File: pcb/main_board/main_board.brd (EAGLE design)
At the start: 72.4 x 72.4 mm, 30 parts, among them J1 5025700893, P1 53398-0510, P2 53398-0810, P3 53398-0410, U1 ATSAMD51J19A-AUT, U13 SPX3819-3.3, X2 32.768, X3 microUSB

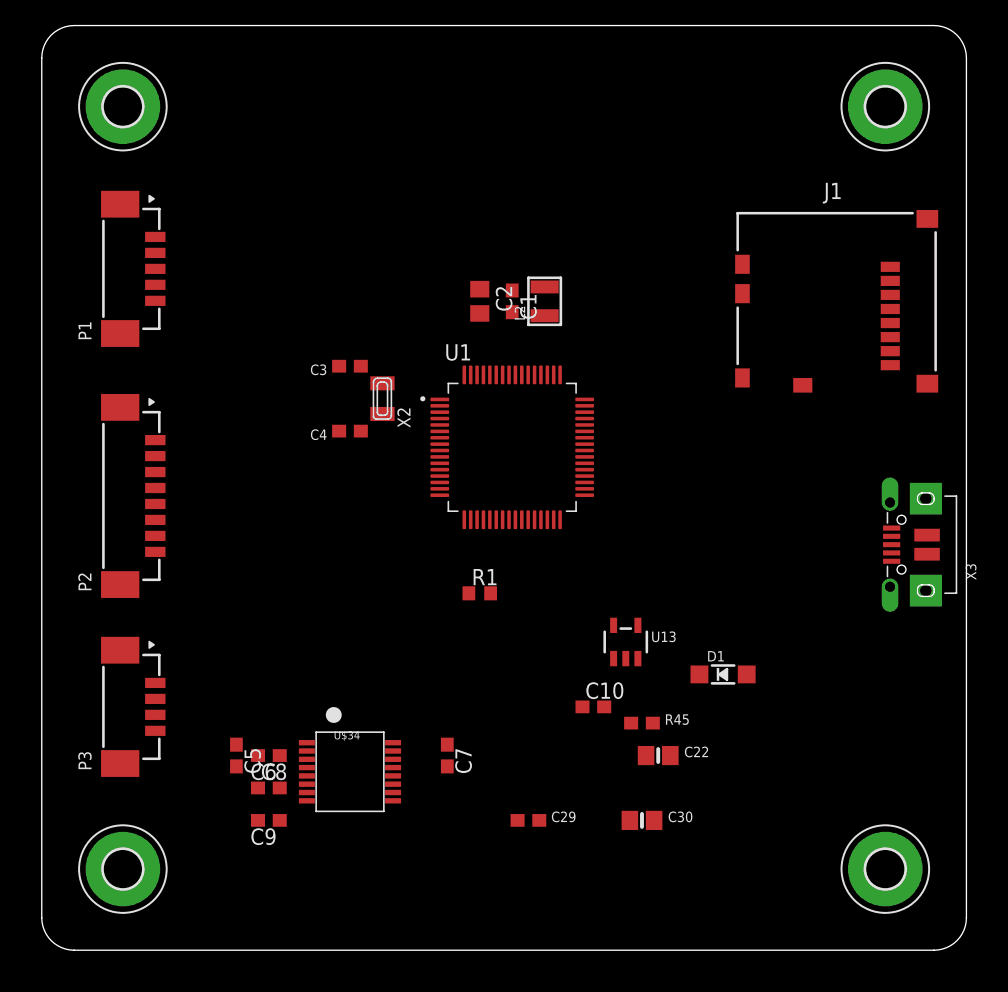
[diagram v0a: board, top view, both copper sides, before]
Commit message: moved to feather wing design
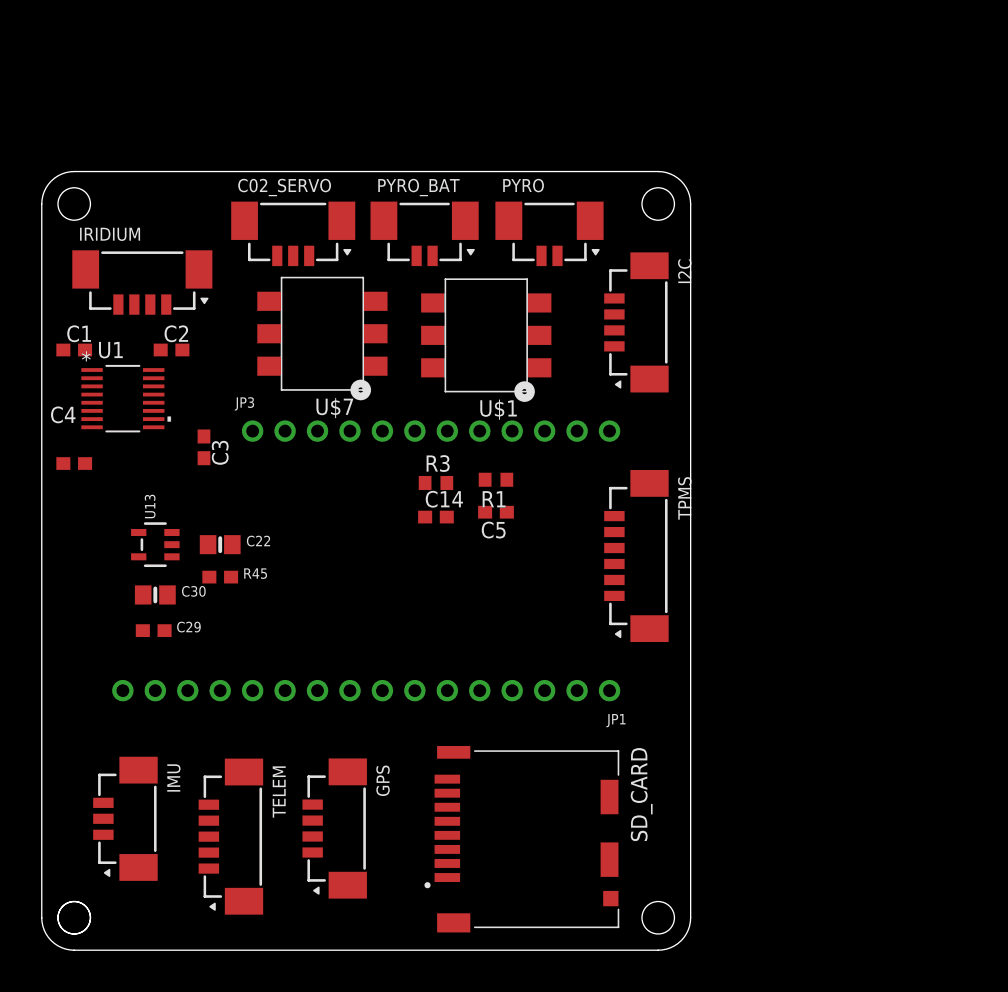
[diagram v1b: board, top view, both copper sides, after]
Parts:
- removed C10: 1uF, rcl:C0603
- removed C6, C7, C8: 0.1uF, rcl:C0603
- removed C9: 0.01uF, rcl:C0603
- removed D1: MBR120, microbuilder:SOD-123
- removed H1, H2, H3, H4: MOUNT-PAD-ROUND3.0, holes:3,0-PAD
- removed J1: 5025700893, 5025700893:MOLEX_5025700893
- removed L2: 10uH, microbuilder:INDUCTOR_1007
- removed P1: 53398-0510, con-molex-picoblade:53398-0510
- removed P2: 53398-0810, con-molex-picoblade:53398-0810
- removed P3: 53398-0410, con-molex-picoblade:53398-0410
- removed U$34: MAX3232E, TI_radio:SSOP-16
- removed X2: 32.768, adafruit2:XTAL3215
- removed X3: microUSB, microbuilder:4UCONN_20329_V2
- added C02_SERVO, IMU: 53398-0310, con-molex-picoblade:53398-0310
- added C14: 0.1uF, adafruit:C0603
- added GPS, I2C, IRIDIUM: 53398-0410, con-molex-picoblade:53398-0410
- added JP1: (no value), microbuilder:1X16_ROUND
- added JP3: (no value), microbuilder:1X12_ROUND
- added PYRO, PYRO_BAT: 53398-0210, con-molex-picoblade:53398-0210
- added R3: 288, adafruit:R0603
- added SD_CARD: DM3CS-SF, DM3CS-SF:HRS_DM3CS-SF
- added TELEM: 53398-0510, con-molex-picoblade:53398-0510
- added TPMS: 53398-0610, con-molex-picoblade:53398-0610
- added U$1, U$7: AQV252GA, TI_radio:DIP6
- C1: value 1uF -> 0.1uF
- C2: value 10uF -> 0.1uF; device rcl:C0805 -> rcl:C0603
- C3, C4: value 22pF -> 0.1uF; device microbuilder:0603-NO -> rcl:C0603
- C5: device rcl:C0603 -> adafruit:C0603
- R1: value 10k -> 288; device rcl:R0603 -> adafruit:R0603
- U1: value ATSAMD51J19A-AUT -> ADM3101EARQZ-REELRQ_16_ADI-L; device ATSAMD51J19A-AUT:QFP50P1200X1200X120-64N -> ADM310:RQ_16_ADI-L
- moved C30 42.0 mm to (8.89, 27.8)
- moved C22 38.1 mm to (14.0, 31.8)
- moved U13 37.6 mm to (8.89, 31.8), turned to 90 degrees
- moved R45 34.9 mm to (14.0, 29.2)
- moved C1 34.5 mm to (2.54, 47.0), turned to 0 degrees
- moved C29 32.9 mm to (8.76, 25.0)
- moved U1 30.7 mm to (6.35, 43.2)
- moved C5 27.9 mm to (35.6, 34.3), turned to 180 degrees
- moved C2 24.4 mm to (10.2, 47.0), turned to 0 degrees
- moved C4 21.7 mm to (2.54, 38.1), turned to 0 degrees
- moved C3 13.1 mm to (12.7, 39.4), turned to 270 degrees
- moved R1 8.98 mm to (35.6, 36.8), turned to 180 degrees
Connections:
- removed net 3.3V: C7.1, U$34.16
- removed net D+: U1.46, X3.D+
- removed net D-: U1.45, X3.D-
- removed net N$11: J1.2
- removed net N$12: J1.1
- removed net N$13: J1.8
- removed net N$14: J1.7
- removed net N$15: P1.2
- removed net N$16: P1.3
- removed net N$17: P1.4
- removed net N$18: P1.5
- removed net N$19: H2.B3,0
- removed net N$2: P1.1
- removed net N$20: H1.B3,0
- removed net N$21: H4.B3,0
- removed net N$22: H3.B3,0
- removed net N$23: P2.1
- removed net N$24: P2.2
- removed net N$25: P2.3
- removed net N$26: P2.4
- removed net N$27: P2.5
- removed net N$28: P2.6
- removed net N$29: P2.7
- removed net N$30: P2.8
- removed net N$31: P3.1
- removed net N$32: P3.2
- removed net N$33: P3.3
- removed net N$34: P3.4
- removed net N$35: C5.1, U$34.1
- removed net N$36: C5.2, U$34.3
- removed net N$37: C8.1, U$34.4
- removed net N$38: C8.2, U$34.5
- removed net N$39: C9.1, U$34.6
- removed net N$40: C6.1, U$34.2
- removed net N$41: C10.2, U1.4
- removed net N$5: C3.1, U1.1, X2.P$1
- removed net QSPI_CS: U1.24
- removed net QSPI_DATA[0]: U1.17
- removed net QSPI_DATA[1]: U1.18
- removed net QSPI_DATA[2]: U1.19
- removed net QSPI_DATA[3]: U1.20
- removed net QSPI_SCK: U1.23
- removed net RX0: U1.40
- removed net SD_DET: J1.10
- removed net SWCLK: U1.57
- removed net SWDIO: U1.58
- removed net TX0: U1.39
- new net !RESET: JP1.16
- new net 3V32: C29.1, C30.1, TELEM.4, U13.5
- new net 9V: PYRO_BAT.1, U$1.6
- new net AREF: JP1.14
- new net CO2_SERVO: C02_SERVO.1, JP3.6
- new net D5: JP3.10
- new net D6: JP3.9
- new net IR_ACT: JP3.7, R3.2
- new net LORA_RST: JP1.12, TELEM.1
- new net MISO: JP1.4, SD_CARD.7
- new net MOSI: JP1.5, SD_CARD.3
- new net N$1: C5.1, R1.1, U$1.1
- new net N$6: C14.1, R3.1, U$7.1
- new net PYRO_ACT: JP3.8, R1.2
- new net RX4: JP1.11, TELEM.3
- new net SCHED: JP1.1, TPMS.2
- new net SCK: JP1.6, SD_CARD.5
- new net SCL: I2C.1, JP3.11
- new net SDA: I2C.2, JP3.12
- new net SD_CS: JP1.7, SD_CARD.2
- new net TX4: JP1.8, TELEM.2
- new net V+_IRIDIUM: IRIDIUM.3, U$7.4
- new net V+_PYRO: PYRO.1, U$1.4
- net 3V3: now also C4.2, GPS.3, I2C.3, JP1.15, SD_CARD.4; no longer C29.1, C30.1, R1.2, U1.21, U1.34, U1.48, U1.56, U13.5
- net EN: now also IMU.1, JP3.2, TPMS.1
- net GND: now also C02_SERVO.3, C14.2, C5.2, GPS.4, I2C.4, IMU.3, IRIDIUM.4, JP1.13, PYRO.2, PYRO_BAT.2, SD_CARD.6, SD_CARD.S1, SD_CARD.S2, SD_CARD.S3, SD_CARD.S5, TELEM.5, TPMS.6, U$1.2, U$7.2, U1.9; no longer C1.2, C10.1, C2.2, C4.2, C6.2, C7.2, C9.2, J1.6, J1.9, R1.1, U$34.15, U1.22, U1.33, U1.47, U1.52, U1.54, U1.7, X3.BASE@1, X3.BASE@2, X3.GND, X3.SPRT@1, X3.SPRT@2, X3.SPRT@3, X3.SPRT@4
- net N$10: now also C2.2, U1.15; no longer J1.3
- net N$3: now also C4.1, U1.7; no longer L2.P$1, U1.55
- net N$4: now also C3.1, U1.10; no longer C1.1, C2.1, L2.P$2, U1.53
- net N$7: now also C2.1, U1.16; no longer C4.1, U1.2, X2.P$2
- net N$8: now also C1.1, U1.2; no longer J1.4
- net N$9: now also C1.2, U1.1; no longer J1.5
- net R232: now also IRIDIUM.2, U1.13; no longer U$34.8
- net RIRI: now also JP3.4, U1.4; no longer U$34.9
- net RX1: now also JP1.3, TPMS.4; no longer U1.12
- net RX2: now also GPS.1, JP1.9; no longer U1.14
- net T232: now also IRIDIUM.1, U1.12; no longer U$34.7
- net TIRI: now also JP3.5, U1.5; no longer U$34.10
- net TX1: now also JP1.2, TPMS.3; no longer U1.11
- net TX2: now also GPS.2, JP1.10; no longer U1.13
- net VBAT: now also C02_SERVO.2, C22.1, IMU.2, JP3.1, R45.1, TPMS.5, U$7.6, U13.1; no longer D1.A
- net VBUS: now also JP3.3; no longer C22.1, D1.C, R45.1, U13.1, X3.VBUS
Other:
- board size 72.4 x 72.4 mm -> 50.8 x 61 mm

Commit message: initial versions of imu logger, cdh, and tpms pcb
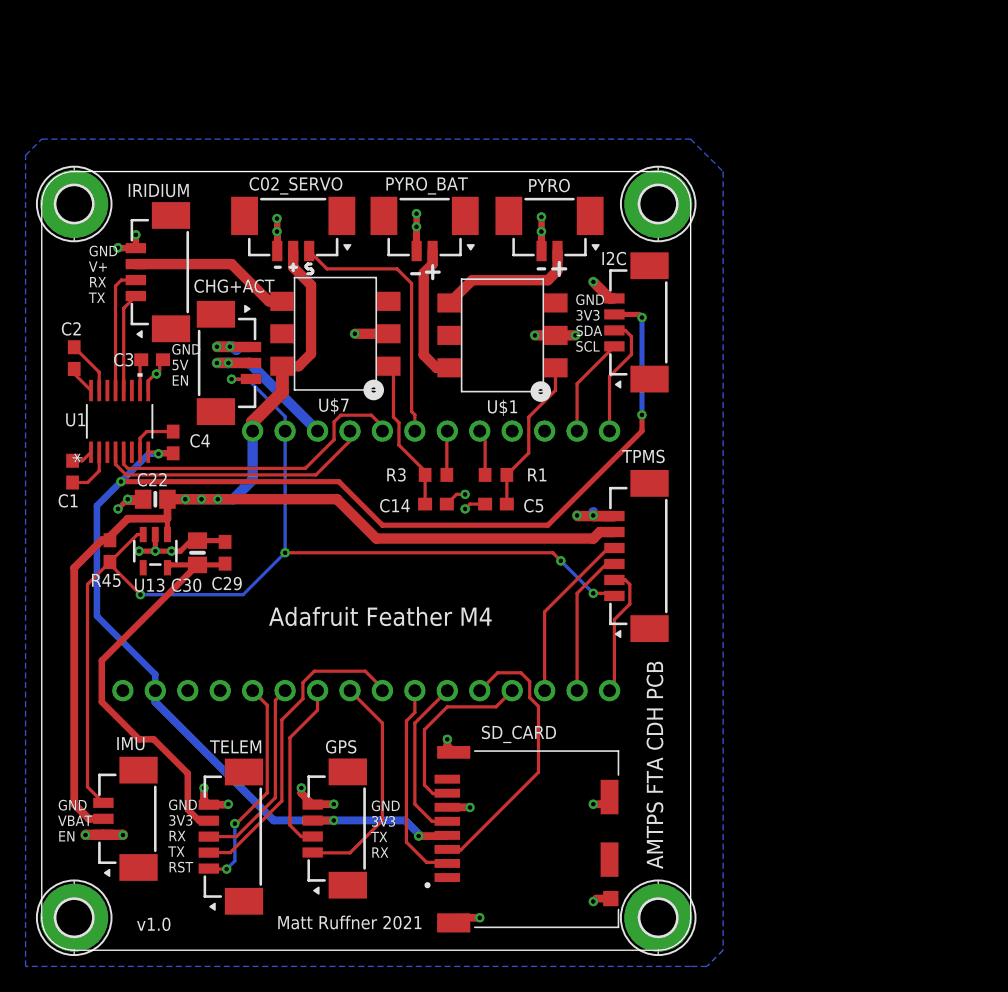
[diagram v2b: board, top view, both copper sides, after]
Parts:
- added CHG+ACT: 53398-0310, con-molex-picoblade:53398-0310
- added H1, H2, H3, H4: MOUNT-PAD-ROUND2.8, holes:2,8-PAD
- moved C1 9.53 mm to (2.41, 37.5), turned to 90 degrees
- moved R45 8.87 mm to (5.33, 31.2), turned to 270 degrees
- moved C29 8.27 mm to (14.4, 31.1), turned to 90 degrees
- moved C3 7.97 mm to (8.64, 46.2), turned to 0 degrees
- moved C4 7.92 mm to (10.3, 39.8), turned to 270 degrees
- moved C2 7.65 mm to (2.54, 46.4), turned to 90 degrees
- moved C22 6.20 mm to (8.89, 35.3), turned to 180 degrees
- moved C30 4.67 mm to (12.2, 31.1), turned to 90 degrees
- moved IRIDIUM 2.59 mm to (7.37, 53.1), turned to 270 degrees
- moved U1 1.80 mm to (6.10, 41.4), turned to 90 degrees
- moved U$1 1.27 mm to (36.1, 48.1)
- moved C14 1.02 mm to (30.9, 34.9)
- moved U$7 1.02 mm to (23.0, 48.3)
- moved C5 0.63 mm to (35.6, 34.9)
- moved R3 0.63 mm to (30.9, 37.2)
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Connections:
- net EN: now also CHG+ACT.3, IMU.3; no longer IMU.1
- net GND: now also CHG+ACT.1, H1.B2,8, H2.B2,8, H3.B2,8, H4.B2,8, IMU.1; no longer IMU.3
- net VBUS: now also CHG+ACT.2
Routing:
- net 3V3: track 0.00 -> 112.4 mm, vias 0 -> 6
- net VBAT: track 0.00 -> 96.6 mm, vias 0 -> 3
- net EN: track 0.00 -> 84.6 mm, vias 0 -> 5
- net GND: track 0.00 -> 71.7 mm, vias 0 -> 35
- net 3V32: track 0.00 -> 32.4 mm
- net TX4: track 0.00 -> 24.7 mm
- net TIRI: track 0.00 -> 24.6 mm
- net MOSI: track 0.00 -> 21.8 mm
- net RIRI: track 0.00 -> 21.5 mm
- net CO2_SERVO: track 0.00 -> 20.7 mm
- net RX2: track 0.00 -> 17.7 mm
- net LORA_RST: track 0.00 -> 17.3 mm, vias 0 -> 2
- net SD_CS: track 0.00 -> 16.0 mm
- net RX4: track 0.00 -> 15.2 mm
- net MISO: track 0.00 -> 14.6 mm
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- added copper zone on layer 16, net GND
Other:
- outline, holes or cut-outs redrawn
- board text added: "AMTPS FTA CDH PCB"
- board text added: "Adafruit Feather M4"
- board text added: "GND 3V3 RX TX RST"
- board text added: "GND 3V3 SDA SCL"
- board text added: "GND 3V3 TX RX"
- board text added: "GND 5V EN"
- board text added: "GND V+ RX TX"
- board text added: "GND VBAT EN"
- board text added: "GND VBAT RX TX SCHED EN"
- board text added: "Matt Ruffner 2021"
- board text added: "v1.0"

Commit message: finished TPMS board and other updates
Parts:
- removed SD_CARD: DM3CS-SF, DM3CS-SF:HRS_DM3CS-SF
- added J1: MEM2067-02-180-00-A_REVB, MEM20267:GCT_MEM2067-02-180-00-A_REVB
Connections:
- net 3V3: now also J1.4; no longer SD_CARD.4
- net GND: now also J1.10, J1.11, J1.12, J1.6, J1.9; no longer SD_CARD.6, SD_CARD.S1, SD_CARD.S2, SD_CARD.S3, SD_CARD.S5
- net MISO: now also J1.7; no longer SD_CARD.7
- net MOSI: now also J1.3; no longer SD_CARD.3
- net SCK: now also J1.5; no longer SD_CARD.5
- net SD_CS: now also J1.2; no longer SD_CARD.2
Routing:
- net GND: track 71.7 -> 78.6 mm, vias 35 -> 39
- net SD_CS: track 16.0 -> 18.5 mm
- net SCK: track 13.0 -> 15.5 mm
- net MISO: track 14.6 -> 17.0 mm
- net 3V3: track 112.4 -> 114.6 mm
- net MOSI: track 21.8 -> 20.3 mm

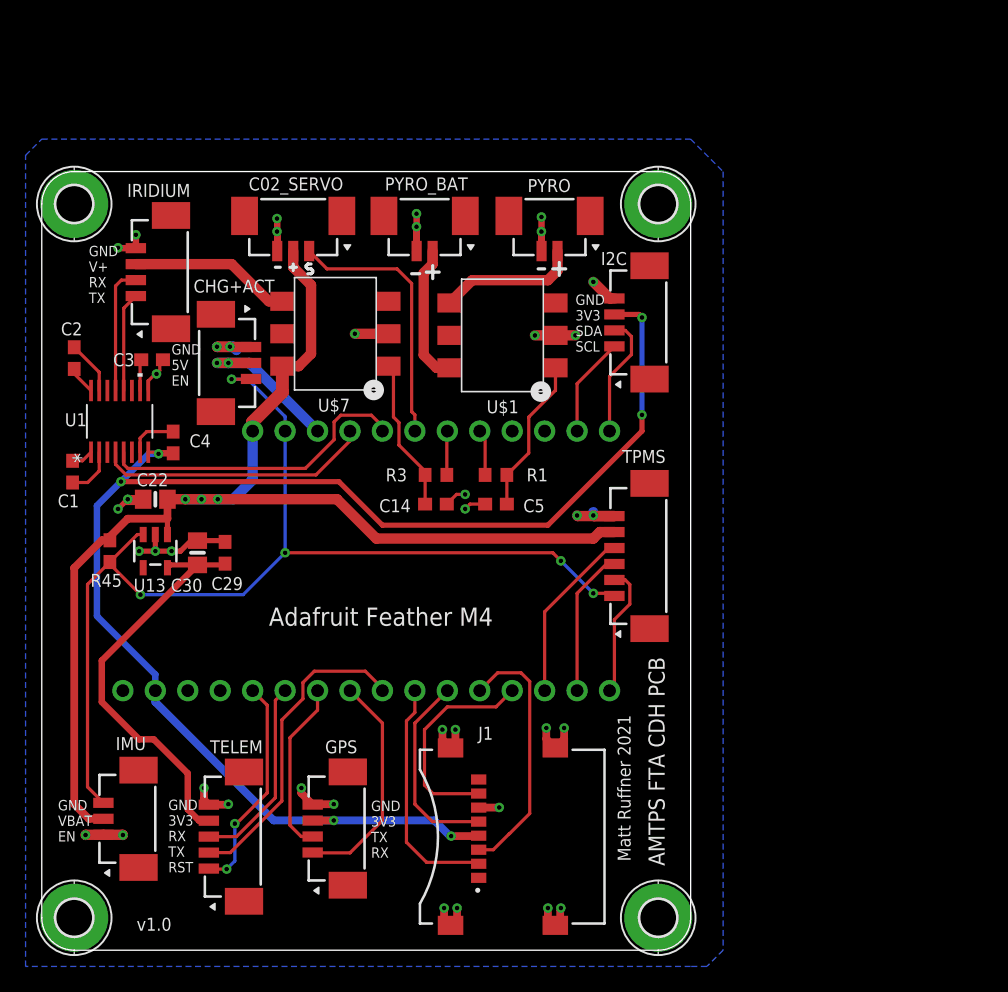
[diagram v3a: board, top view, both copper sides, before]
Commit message: updated main board to have new rs232 transceiver and optional mosfets for pyro and iridium power control
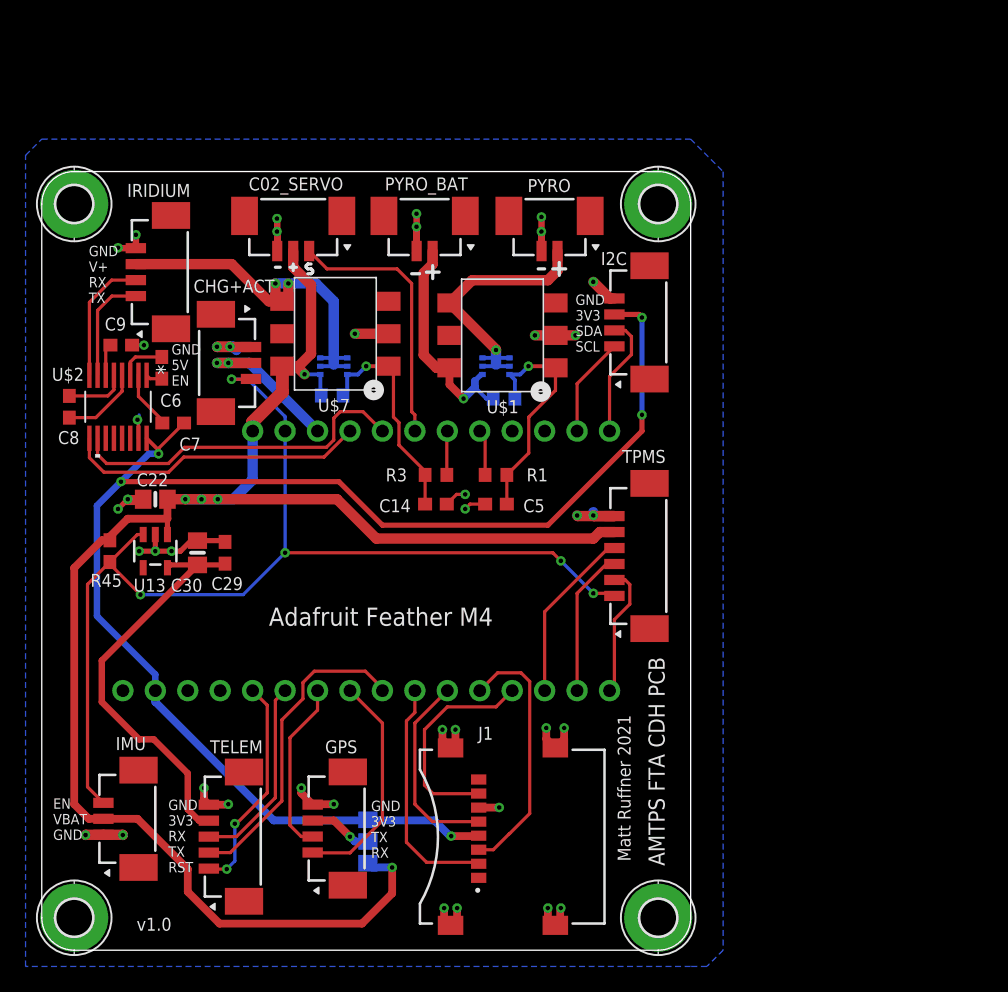
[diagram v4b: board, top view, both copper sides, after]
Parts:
- removed C1, C2, C3, C4: 0.1uF, rcl:C0603
- removed U1: ADM3101EARQZ-REELRQ_16_ADI-L, ADM310:RQ_16_ADI-L
- added C6, C7, C8, C9: 0.1uF, rcl:C0603
- added JMP1: 0R-JUMPA, jump-0r-smd:A0R-JMP
- added R2, R4: 288, adafruit:R0603
- added U$2: UM3232EEAE, ADM310:RQ_16_ADI
- added U2, U3: SSM6J414TU, ssm6j414tu:UF6_TOS
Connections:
- removed net N$10: C2.2, U1.15
- removed net N$3: C4.1, U1.7
- removed net N$4: C3.1, U1.10
- removed net N$7: C2.1, U1.16
- removed net N$8: C1.1, U1.2
- removed net N$9: C1.2, U1.1
- new net N$11: C7.1, U$2.2
- new net N$12: C6.1, U$2.3
- new net N$13: C8.2, U$2.4
- new net N$14: C8.1, U$2.5
- new net N$15: C9.2, U$2.6
- new net N$2: GPS.3, JMP1.2
- new net N$5: C6.2, U$2.1
- net 3V3: now also C7.2, JMP1.3, U$2.16; no longer C4.2, GPS.3, U1.8
- net 9V: now also R4.2, U2.4
- net GND: now also C9.1, U$2.15; no longer C3.2, U1.9
- net N$1: now also R4.1, U2.3
- net N$6: now also R2.1, U3.3
- net R232: now also U$2.8; no longer U1.13
- net RIRI: now also U$2.9; no longer U1.4
- net T232: now also U$2.7; no longer U1.12
- net TIRI: now also U$2.10; no longer U1.5
- net V+_IRIDIUM: now also U3.1, U3.2, U3.5, U3.6
- net V+_PYRO: now also U2.1, U2.2, U2.5, U2.6
- net VBAT: now also JMP1.1, R2.2, U3.4
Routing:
- net VBAT: track 96.6 -> 133.6 mm, vias 3 -> 5
- net V+_IRIDIUM: track 12.7 -> 30.4 mm, vias 0 -> 2
- net V+_PYRO: track 11.0 -> 21.7 mm, vias 0 -> 1
- net 9V: track 10.9 -> 18.1 mm, vias 0 -> 1
- net N$13: track 0.00 -> 6.24 mm
- net N$1: track 12.2 -> 18.2 mm, vias 0 -> 1
- net N$6: track 12.0 -> 17.3 mm, vias 0 -> 1
- net N$2: track 0.00 -> 5.01 mm, vias 0 -> 1
- net N$14: track 0.00 -> 4.82 mm
- net N$11: track 0.00 -> 4.51 mm
- net N$10: track 4.20 -> 0.00 mm
- net N$8: track 3.93 -> 0.00 mm
- net N$3: track 3.90 -> 0.00 mm
- net N$12: track 0.00 -> 3.67 mm
- net TIRI: track 24.6 -> 27.2 mm
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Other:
- board text added: "EN VBAT GND"
- board text removed: "GND VBAT EN"
